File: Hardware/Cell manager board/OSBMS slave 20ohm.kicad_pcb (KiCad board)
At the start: 2 copper layers, 49 x 49 mm, 73 parts, among them P1 CONN_01X07, P2 EXT-TMP, P3 CONN_01X09, P4 CONN_01X09, Q1 BSS138, Q2 BSS138, Q3 BSS138, Q4 BSS138, Q5 BSS138, Q6 BSS138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

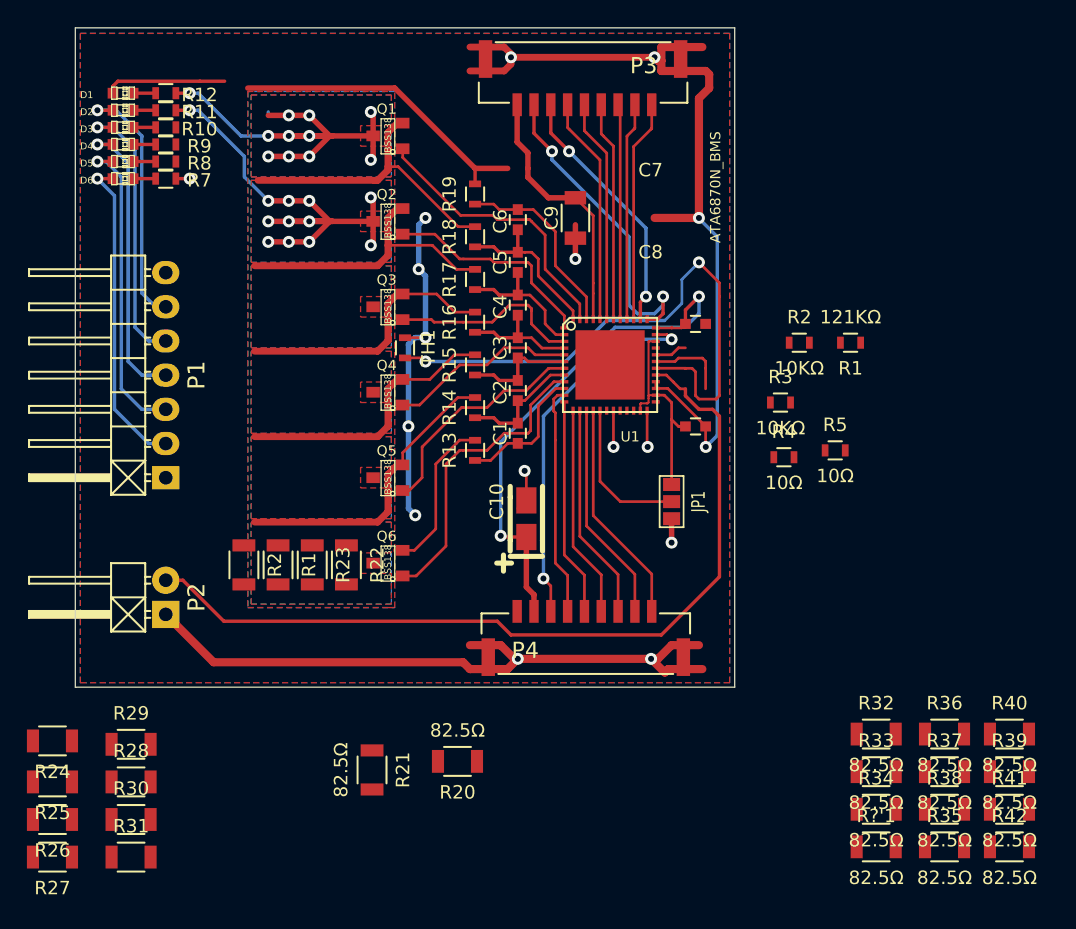
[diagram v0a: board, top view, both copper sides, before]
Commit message: changed design to use better resistors
revamped design to use more commonly avalable resistors and resistor
packs that should protect the mosfet gates in the event of a voltage
spike etc.  also improved thermal design. some thermal stitching still
has to be done but is quite tedious
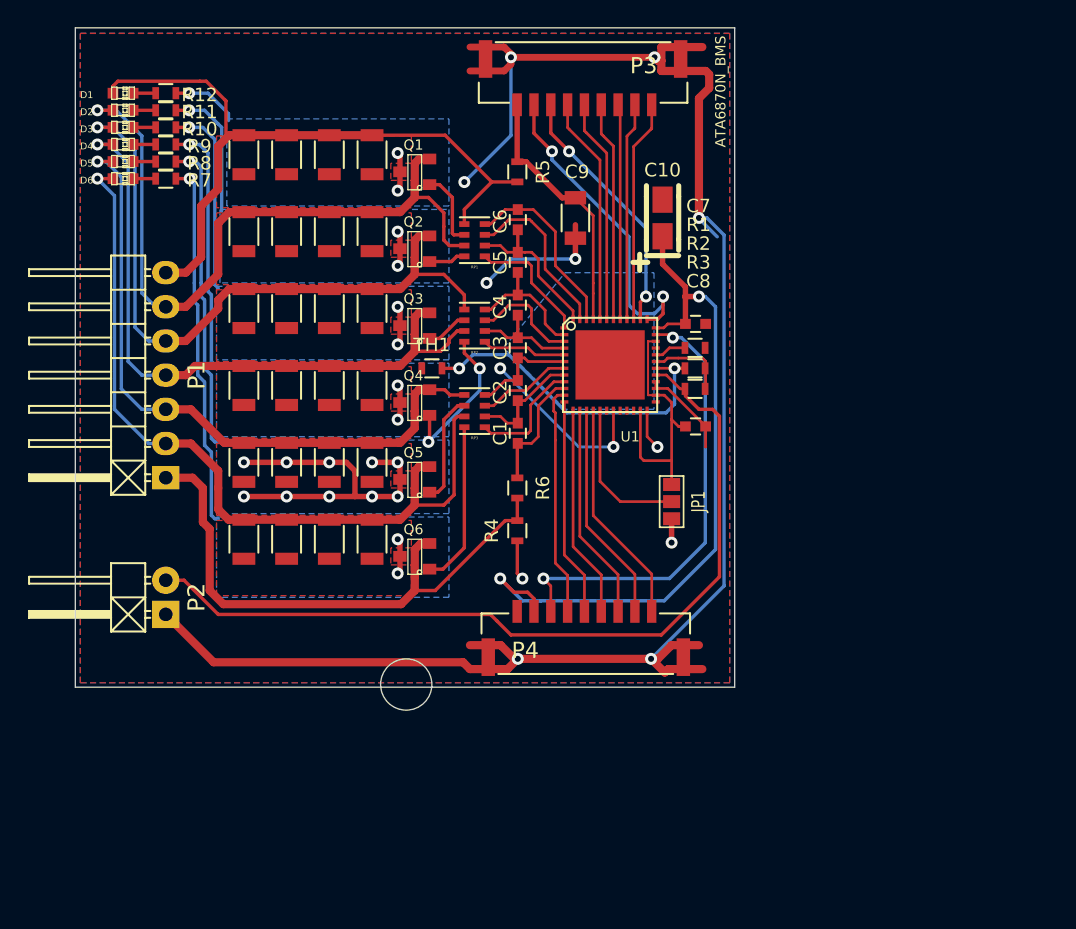
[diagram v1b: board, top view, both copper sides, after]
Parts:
- removed the R1 at (181.1, 144.9)
- removed R14, R15, R16, R17, R18, R19: 1KΩ, Resistors_SMD:R_0603
- removed the R2 at (178.5, 144.9)
- removed R?'1: 82.5Ω, Resistors_SMD:R_1206
- added R6: 1K, Resistors_SMD:R_0603, F.Cu at (198.8, 139.2)
- added RP1: 1K_PACK, Resistors_SMD:R_Cat16-4, F.Cu at (195.7, 120.8)
- added RP2: 1K_PACK, Resistors_SMD:R_Cat16-4, F.Cu at (195.7, 127.1)
- added RP3: 1K_PACK, Resistors_SMD:R_Cat16-4, F.Cu at (195.7, 133.5)
- R13: value 1KΩ -> 82.5Ω; footprint Resistors_SMD:R_0603 -> Resistors_SMD:R_1206
- moved R42 61.3 mm to (178.5, 143.0), turned to 270 degrees
- moved R41 57.3 mm to (181.7, 143.0), turned to 270 degrees
- moved R36 55.8 mm to (178.5, 137.3), turned to 270 degrees
- moved R37 54.0 mm to (181.7, 137.3), turned to 270 degrees
- moved R34 54.0 mm to (181.7, 131.6), turned to 270 degrees
- moved R39 53.4 mm to (184.9, 143.0), turned to 270 degrees
- moved R38 52.5 mm to (184.9, 137.3), turned to 270 degrees
- moved R27 52.2 mm to (188.1, 120.1), turned to 270 degrees
- moved R35 51.3 mm to (188.1, 137.3), turned to 270 degrees
- moved R33 49.8 mm to (184.9, 131.6), turned to 270 degrees
- moved R40 49.5 mm to (188.1, 143.0), turned to 270 degrees
- moved R26 48.3 mm to (184.9, 120.1), turned to 270 degrees
- moved R20 46.8 mm to (181.7, 114.4), turned to 270 degrees
- moved R21 46.7 mm to (178.5, 114.4)
- moved R32 45.6 mm to (188.1, 131.6), turned to 270 degrees
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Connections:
- Q1 pad 1: /DISCH6 -> Net-(Q1-Pad1)
- Q2 pad 1: /DISCH5 -> Net-(Q2-Pad1)
- Q3 pad 1: /DISCH4 -> Net-(Q3-Pad1)
- Q4 pad 1: /DISCH3 -> Net-(Q4-Pad1)
- Q5 pad 1: /DISCH2 -> Net-(Q5-Pad1)
- Q6 pad 1: /DISCH1 -> Net-(Q6-Pad1)
- R13 pad 1: Net-(C1-Pad2) -> Net-(D4-Pad1)
- R13 pad 2: Net-(P1-Pad1) -> Net-(Q4-Pad3)
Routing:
- net Net-(Q5-Pad3): track 0.00 -> 49.6 mm, vias 0 -> 11
- net Net-(P1-Pad1): track 12.0 -> 42.8 mm
- net Net-(Q6-Pad3): track 1.16 -> 30.3 mm, vias 1 -> 3
- net Net-(Q1-Pad3): track 35.0 -> 7.99 mm, vias 11 -> 3
- net Net-(Q2-Pad3): track 37.4 -> 12.8 mm, vias 12 -> 3
- net Net-(Q4-Pad3): track 0.00 -> 21.5 mm, vias 0 -> 3
- net Net-(D1-Pad1): track 31.9 -> 52.8 mm
- net GND: track 154.6 -> 175.3 mm, vias 16 -> 13
- net Net-(R2-Pad2): track 43.4 -> 25.4 mm
- net Net-(Q3-Pad3): track 0.00 -> 17.4 mm, vias 0 -> 3
- net +3.3V: track 39.5 -> 53.7 mm
- net /DISCH1: track 22.7 -> 8.80 mm
- net Net-(D6-Pad1): track 46.3 -> 60.1 mm
- net Net-(Q6-Pad1): track 0.00 -> 12.2 mm
- net Net-(D2-Pad1): track 41.6 -> 53.4 mm
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- added copper zone on B.Cu, net (none)
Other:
- board size 49 x 49 mm -> 49 x 50.7 mm

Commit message: finished resistor change and via stiching
finished resistor change and via stiching. board is now functional (at
least I hope) the last thing to do is tidy up the silkscreen and
soldermask
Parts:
- added 28 mil Id via: via, MasCustomParts:35-Od-28mil-Id-via, F.Cu at (205.7, 130.1)
- added 28 mil Id via: via, MasCustomParts:35-Od-28mil-Id-via, F.Cu at (204.3, 128.7)
- added 28 mil Id via: via, MasCustomParts:35-Od-28mil-Id-via, F.Cu at (207.1, 131.4)
- added 28 mil Id via: via, MasCustomParts:35-Od-28mil-Id-via, F.Cu at (204.3, 131.4)
- added 28 mil Id via: via, MasCustomParts:35-Od-28mil-Id-via, F.Cu at (207.1, 128.7)
- added P5: CONN_01X01, SMD_Packages:1Pin, B.Cu at (205.7, 130.1)
- Q1, Q2, Q3, Q4, Q5, Q6: footprint SMD_Packages:SOT-23 -> SOT-23
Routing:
- net Net-(Q4-Pad3): track 21.5 -> 74.4 mm, vias 3 -> 23
- net Net-(Q2-Pad3): track 12.8 -> 63.0 mm, vias 3 -> 21
- net Net-(Q3-Pad3): track 17.4 -> 67.3 mm, vias 3 -> 21
- net Net-(Q1-Pad3): track 7.99 -> 57.9 mm, vias 3 -> 21
- net Net-(Q6-Pad3): track 30.3 -> 80.2 mm, vias 3 -> 21
- net Net-(Q5-Pad3): track 49.6 -> 76.0 mm, vias 11 -> 21
- net GND: track 175.3 -> 178.3 mm
- added copper zone on B.Cu, net ThermalGnd
- removed copper zone on B.Cu, net (none)
